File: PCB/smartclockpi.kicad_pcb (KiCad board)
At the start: 2 copper layers, 94.5 x 67.1 mm, 29 parts, among them J1 Raspberry_Pi, J2 DS3231 RTC module, J3 ILI9488 SPI TFT touchscreen, J5 USB_B_Micro, J6 USB_A, J7 microUSB IN, J8 USB-A OUT, J9 PWR IN, U2 MCP3008, U3 DHT22

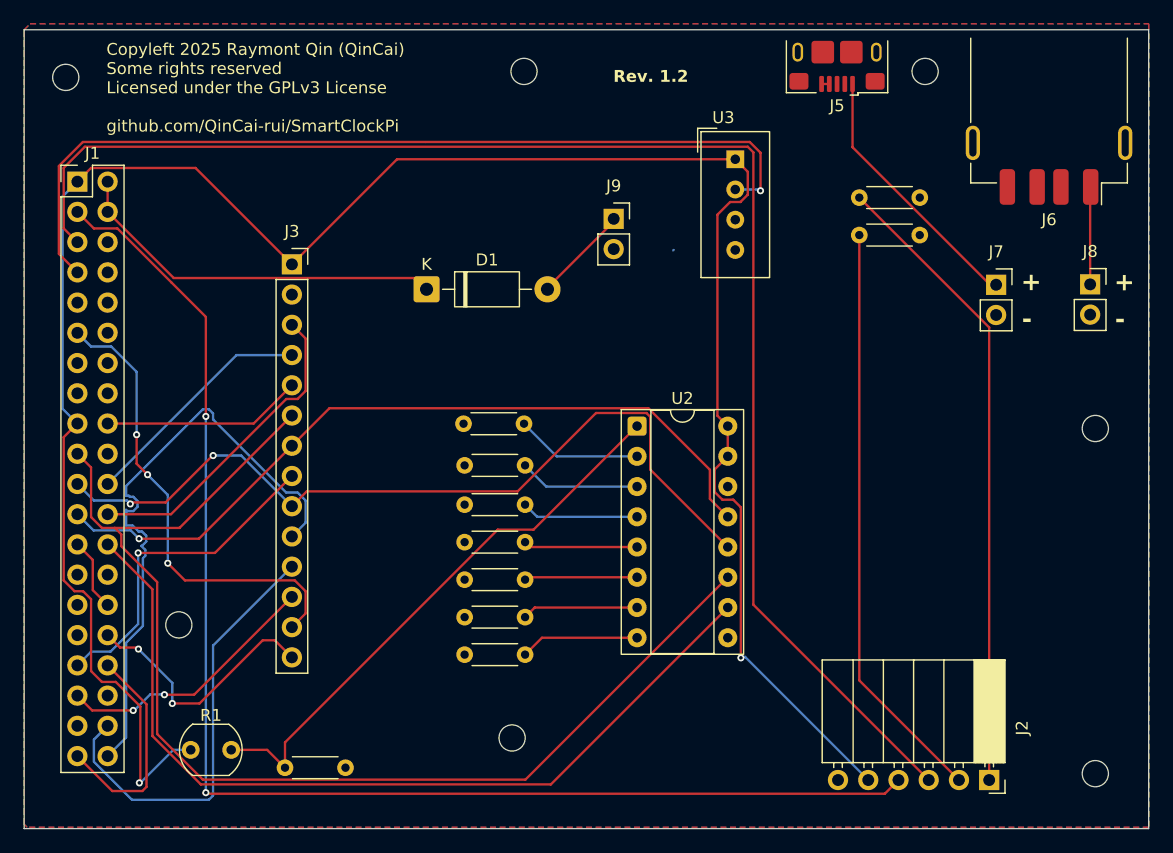
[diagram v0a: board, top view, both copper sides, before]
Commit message: fix PCB issues and re-gen everything needed
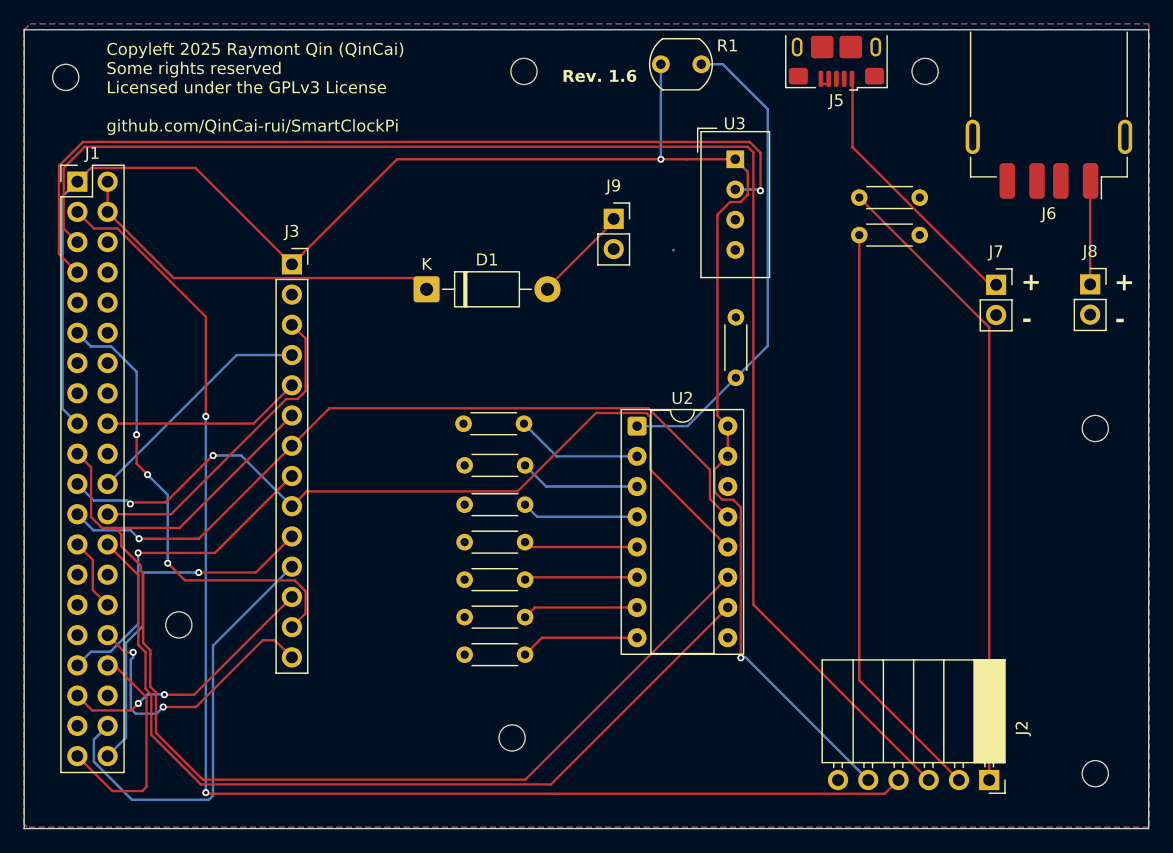
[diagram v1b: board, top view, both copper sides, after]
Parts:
- moved R1 69.8 mm to (93.5, 71.9)
- moved R2 50.1 mm to (99.8, 98.2), turned to 90 degrees
- moved J6 0.51 mm to (126.1, 74.5)
- moved J5 0.43 mm to (108.2, 70.5)
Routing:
- net +3.3V: track 185.3 -> 153.4 mm
- net Net-(J1-GPIO21/SCLK1): track 51.9 -> 30.4 mm, vias 0 -> 1
- net Net-(U2-CH0): track 47.9 -> 40.8 mm
- net Net-(J1-PWM0/GPIO12): track 21.7 -> 24.4 mm
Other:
- board text added: "Rev. 1.6"
- board text removed: "Rev. 1.2"

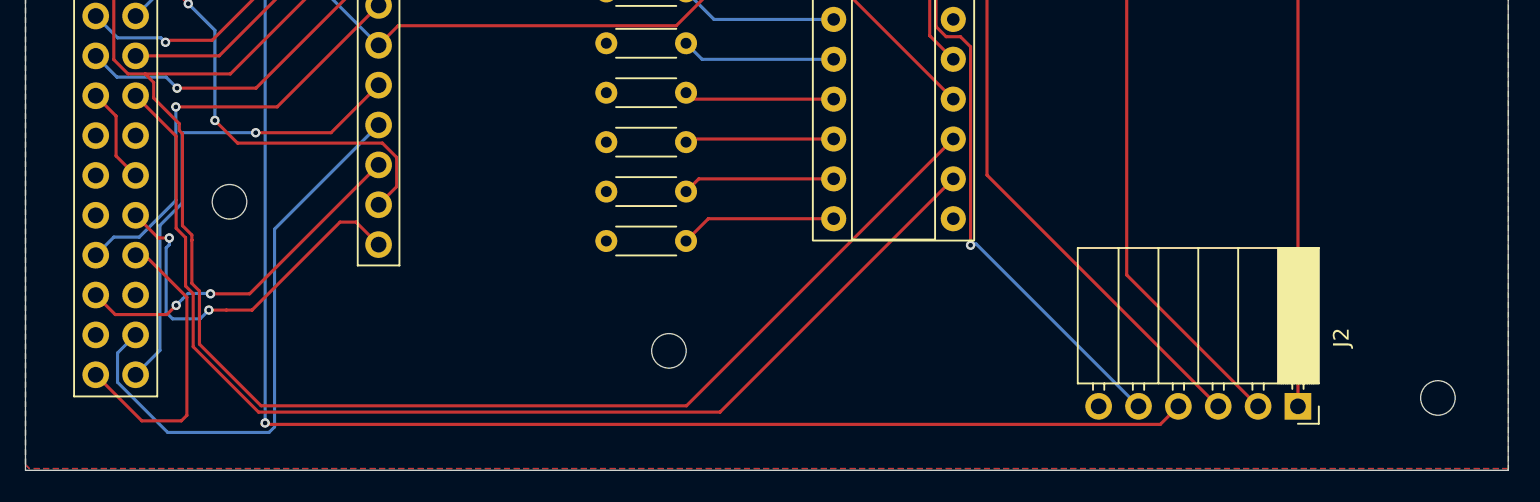
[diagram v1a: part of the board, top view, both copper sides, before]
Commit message: fix some DRC errors. regen models
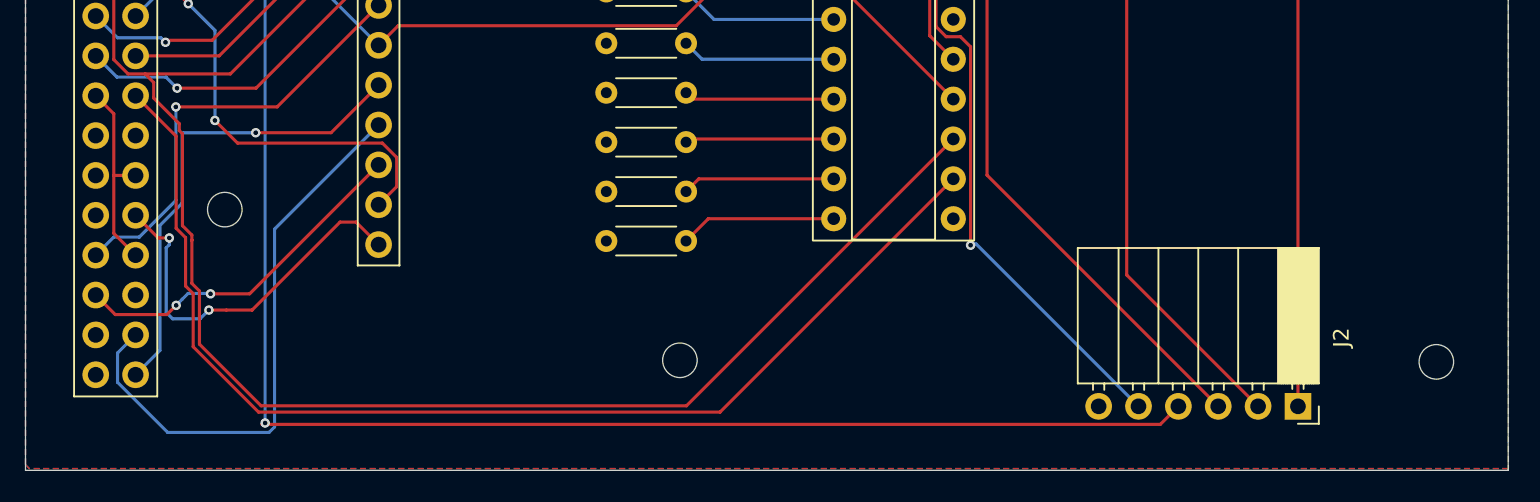
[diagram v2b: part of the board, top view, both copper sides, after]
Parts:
- moved REF** 2.30 mm to (129.9, 129.2)
- moved REF** 0.92 mm to (81.7, 129.1)
- moved REF** 0.58 mm to (52.7, 119.5)
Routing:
- net GND: track 26.4 -> 14.4 mm
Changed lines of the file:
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@@
 	(footprint "MountingHole:MountingHole_2.2mm_M2"
 		(layer "F.Cu")
-		(at 53 119)
+		(at 52.7 119.5)
 		(descr "Mounting Hole 2.2mm, M2, no annular, generated by kicad-footprint-generator mountinghole.py")
 		(tags "mountinghole M2")
@@
 	(footprint "MountingHole:MountingHole_2.2mm_M2"
 		(layer "F.Cu")
-		(at 81 128.5)
+		(at 81.7 129.1)
 		(descr "Mounting Hole 2.2mm, M2, no annular, generated by kicad-footprint-generator mountinghole.py")
 		(tags "mountinghole M2")
@@
 	(footprint "MountingHole:MountingHole_2.2mm_M2"
 		(layer "F.Cu")
+		(at 129.9 129.2)
+		(descr "Mounting Hole 2.2mm, M2, no annular, generated by kicad-footprint-generator mountinghole.py")
+		(tags "mountinghole M2")
+		(property "Reference" "REF**"
+			(at 0 -3.15 0)
+			(layer "F.SilkS")
+			(hide yes)
+			(effects
+				(font
+					(size 1 1)
+					(thickness 0.15)
+				)
+			)
+		)
+		(property "Value" "MountingHole_2.2mm_M2"
+			(at 0 3.15 0)
+			(layer "F.Fab")
+			(hide yes)
+			(effects
+				(font
+					(size 1 1)
+					(thickness 0.15)
+				)
+			)
+		)
+		(property "Datasheet" ""
+			(at 0 0 0)
+			(layer "F.Fab")
+			(hide yes)
+			(effects
+				(font
+					(size 1.27 1.27)
+					(thickness 0.15)
+				)
+			)
+		)
+		(property "Description" ""
+			(at 0 0 0)
+			(layer "F.Fab")
+			(hide yes)
+			(effects
+				(font
+					(size 1.27 1.27)
+					(thickness 0.15)
+				)
+			)
+		)
+		(attr exclude_from_pos_files exclude_from_bom)
+		(fp_circle
+			(center 0 0)
+			(end 2.2 0)
+			(stroke
+				(width 0.15)
+				(type solid)
+			)
+			(fill no)
+			(layer "Cmts.User")
+		)
+		(fp_circle
+			(center 0 0)
+			(end 2.45 0)
+			(stroke
+				(width 0.05)
+				(type solid)
+			)
+			(fill no)
+			(layer "F.CrtYd")
+		)
+		(fp_text user "${REFERENCE}"
+			(at 0 0 0)
+			(layer "F.Fab")
+			(effects
+				(font
+					(size 1 1)
+					(thickness 0.15)
+				)
+			)
+		)
+		(pad "" np_thru_hole circle
+			(at 0 0)
+			(size 2.2 2.2)
+			(drill 2.2)
+			(layers "*.Cu" "*.Mask")
+		)
+		(embedded_fonts no)
+	)
+	(footprint "MountingHole:MountingHole_2.2mm_M2"
+		(layer "F.Cu")
 		(at 43.5 73)
 		(descr "Mounting Hole 2.2mm, M2, no annular, generated by kicad-footprint-generator mountinghole.py")
@@
 		(embedded_fonts no)
 	)
-	(footprint "MountingHole:MountingHole_2.2mm_M2"
-		(layer "F.Cu")
-		(at 130 131.5)
-		(descr "Mounting Hole 2.2mm, M2, no annular, generated by kicad-footprint-generator mountinghole.py")
-		(tags "mountinghole M2")
-		(property "Reference" "REF**"
-			(at 0 -3.15 0)
-			(layer "F.SilkS")
-			(hide yes)
-			(effects
-				(font
-					(size 1 1)
-					(thickness 0.15)
-				)
-			)
-		)
-		(property "Value" "MountingHole_2.2mm_M2"
-			(at 0 3.15 0)
-			(layer "F.Fab")
-			(hide yes)
-			(effects
-				(font
-					(size 1 1)
-					(thickness 0.15)
-				)
-			)
-		)
-		(property "Datasheet" ""
-			(at 0 0 0)
-			(layer "F.Fab")
-			(hide yes)
-			(effects
-				(font
-					(size 1.27 1.27)
-					(thickness 0.15)
-				)
-			)
-		)
-		(property "Description" ""
-			(at 0 0 0)
-			(layer "F.Fab")
-			(hide yes)
-			(effects
-				(font
-					(size 1.27 1.27)
-					(thickness 0.15)
-				)
-			)
-		)
-		(attr exclude_from_pos_files exclude_from_bom)
-		(fp_circle
-			(center 0 0)
-			(end 2.2 0)
-			(stroke
-				(width 0.15)
-				(type solid)
-			)
-			(fill no)
-			(layer "Cmts.User")
-		)
-		(fp_circle
-			(center 0 0)
-			(end 2.45 0)
-			(stroke
-				(width 0.05)
-				(type solid)
-			)
-			(fill no)
-			(layer "F.CrtYd")
-		)
-		(fp_text user "${REFERENCE}"
-			(at 0 0 0)
-			(layer "F.Fab")
-			(effects
-				(font
-					(size 1 1)
-					(thickness 0.15)
-				)
-			)
-		)
-		(pad "" np_thru_hole circle
-			(at 0 0)
-			(size 2.2 2.2)
-			(drill 2.2)
-			(layers "*.Cu" "*.Mask")
-		)
-		(embedded_fonts no)
-	)
 	(gr_rect
 		(start 40 69)
@@
 	)
 	(segment
-		(start 45.7708 116.078)
-		(end 45.7708 113.538)
+		(start 47.0154 122.4026)
+		(end 47.6026 122.4026)
 		(width 0.2)
 		(layer "F.Cu")
@@
 	)
 	(segment
-		(start 47.0154 122.4026)
-		(end 47.6026 122.4026)
+		(start 45.6264 117.35)
+		(end 45.6264 113.3936)
 		(width 0.2)
 		(layer "F.Cu")
@@
 	)
 	(segment
-		(start 47.0154 117.3226)
-		(end 45.7708 116.078)
+		(start 45.6264 113.3936)
+		(end 44.4754 112.2426)
 		(width 0.2)
 		(layer "F.Cu")
@@
 	)
 	(segment
-		(start 45.7708 113.538)
-		(end 44.4754 112.2426)
+		(start 45.6264 121.0136)
+		(end 45.6264 117.35)
 		(width 0.2)
 		(layer "F.Cu")
@@
 	)
 	(segment
-		(start 49.931343 132.9604)
-		(end 47.4132 132.9604)
+		(start 45.6538 117.3226)
+		(end 45.6264 117.35)
 		(width 0.2)
 		(layer "F.Cu")
@@
 	)
 	(segment
-		(start 47.4132 132.9604)
-		(end 44.4754 130.0226)
-		(width 0.2)
-		(layer "F.Cu")
-		(net 1)
-	)
-	(segment
-		(start 47.6026 122.4026)
-		(end 50.2834 125.0834)
-		(width 0.2)
-		(layer "F.Cu")
-		(net 1)
-	)
-	(segment
-		(start 50.2834 125.0834)
-		(end 50.2834 132.608343)
+		(start 47.0154 122.4026)
+		(end 45.6264 121.0136)
 		(width 0.2)
 		(layer "F.Cu")
@@
 	)
 	(segment
-		(start 50.2834 132.608343)
-		(end 49.931343 132.9604)
+		(start 47.0154 117.3226)
+		(end 45.6538 117.3226)
 		(width 0.2)
 		(layer "F.Cu")

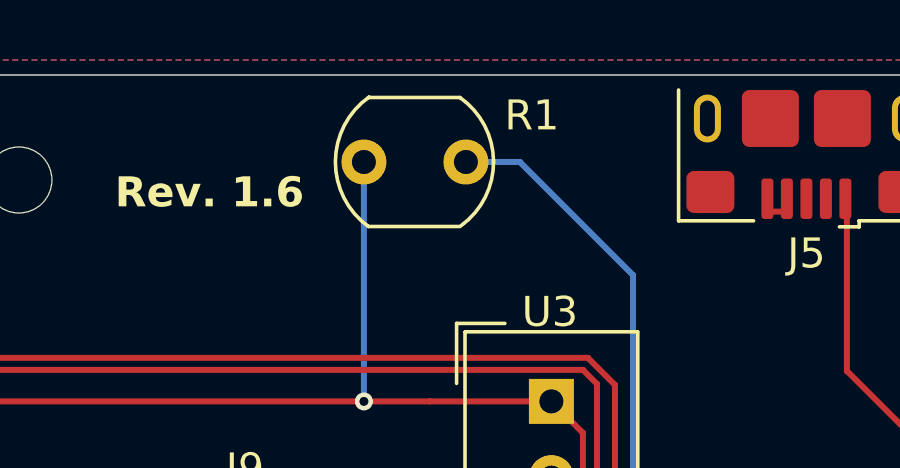
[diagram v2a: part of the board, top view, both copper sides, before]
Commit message: update footprint for LDR. re-gen models
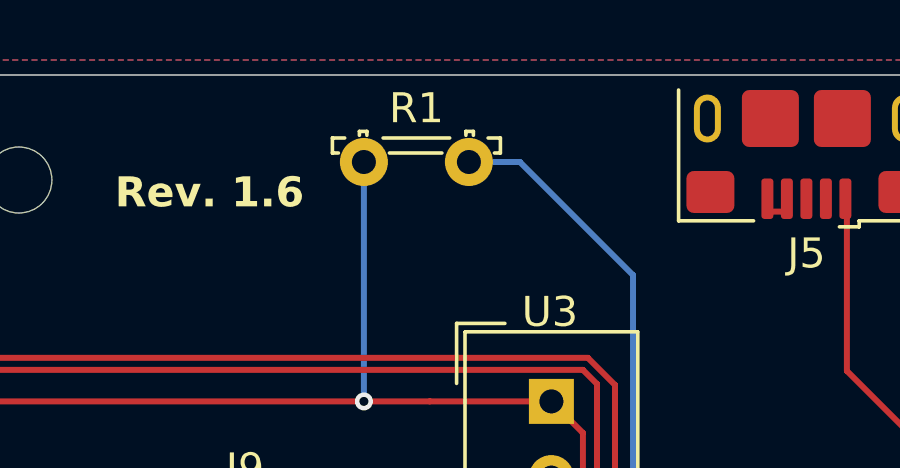
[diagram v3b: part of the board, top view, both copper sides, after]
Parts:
- R1: footprint OptoDevice:R_LDR_5.1x4.3mm_P3.4mm_Vertical -> OptoDevice:R_LDR_5.2x5.2mm_P3.5mm_Horizontal
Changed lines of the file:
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@@
 		)
 	)
-	(footprint "OptoDevice:R_LDR_5.1x4.3mm_P3.4mm_Vertical"
+	(footprint "OptoDevice:R_LDR_5.2x5.2mm_P3.5mm_Horizontal"
 		(layer "F.Cu")
 		(at 93.5 71.9)
-		(descr "Resistor, LDR 5.1x3.4mm, see http://yourduino.com/docs/Photoresistor-5516-datasheet.pdf")
-		(tags "Resistor LDR5.1x3.4mm")
+		(descr "Resistor, LDR 5.2x5.2, upright, see http://cdn-reichelt.de/documents/datenblatt/A500/M996011A.pdf")
+		(tags "Resistor LDR5.2x5.2 ")
 		(property "Reference" "R1"
-			(at 5.6 -1.55 0)
+			(at 1.75 -1.79 0)
 			(layer "F.SilkS")
 			(effects
@@
 		)
 		(property "Value" "LDR07"
-			(at 1.5 3 0)
+			(at 1.62 1.4 0)
 			(layer "F.Fab")
 			(effects
@@
 		(attr through_hole)
 		(fp_line
-			(start 0.15 -2.15)
-			(end 3.2 -2.15)
-			(stroke
-				(width 0.12)
-				(type solid)
-			)
-			(layer "F.SilkS")
-		)
-		(fp_line
-			(start 0.15 2.15)
-			(end 3.2 2.15)
-			(stroke
-				(width 0.12)
-				(type solid)
-			)
-			(layer "F.SilkS")
-		)
-		(fp_arc
-			(start 0.15 2.15)
-			(mid -0.950438 -0.013368)
-			(end 0.171766 -2.165525)
-			(stroke
-				(width 0.12)
-				(type solid)
-			)
-			(layer "F.SilkS")
-		)
-		(fp_arc
-			(start 3.2 -2.15)
-			(mid 4.321403 -0.027338)
-			(end 3.244513 2.118249)
-			(stroke
-				(width 0.12)
-				(type solid)
-			)
-			(layer "F.SilkS")
-		)
-		(fp_line
-			(start -1.13 -2.35)
-			(end -1.13 2.35)
+			(start -1.05 -0.8)
+			(end -1.05 -0.3)
+			(stroke
+				(width 0.12)
+				(type solid)
+			)
+			(layer "F.SilkS")
+		)
+		(fp_line
+			(start -1.05 -0.3)
+			(end -0.85 -0.3)
+			(stroke
+				(width 0.12)
+				(type solid)
+			)
+			(layer "F.SilkS")
+		)
+		(fp_line
+			(start -0.64 -0.8)
+			(end -1.05 -0.8)
+			(stroke
+				(width 0.12)
+				(type solid)
+			)
+			(layer "F.SilkS")
+		)
+		(fp_line
+			(start -0.15 -1.02)
+			(end -0.15 -0.89)
+			(stroke
+				(width 0.12)
+				(type solid)
+			)
+			(layer "F.SilkS")
+		)
+		(fp_line
+			(start -0.15 -1.02)
+			(end 0.1 -1.02)
+			(stroke
+				(width 0.12)
+				(type solid)
+			)
+			(layer "F.SilkS")
+		)
+		(fp_line
+			(start 0.1 -1.02)
+			(end 0.1 -0.89)
+			(stroke
+				(width 0.12)
+				(type solid)
+			)
+			(layer "F.SilkS")
+		)
+		(fp_line
+			(start 0.85 -0.3)
+			(end 2.6 -0.3)
+			(stroke
+				(width 0.12)
+				(type solid)
+			)
+			(layer "F.SilkS")
+		)
+		(fp_line
+			(start 2.86 -0.8)
+			(end 0.64 -0.8)
+			(stroke
+				(width 0.12)
+				(type solid)
+			)
+			(layer "F.SilkS")
+		)
+		(fp_line
+			(start 3.4 -1.02)
+			(end 3.4 -0.89)
+			(stroke
+				(width 0.12)
+				(type solid)
+			)
+			(layer "F.SilkS")
+		)
+		(fp_line
+			(start 3.4 -1.02)
+			(end 3.65 -1.02)
+			(stroke
+				(width 0.12)
+				(type solid)
+			)
+			(layer "F.SilkS")
+		)
+		(fp_line
+			(start 3.65 -1.02)
+			(end 3.65 -0.89)
+			(stroke
+				(width 0.12)
+				(type solid)
+			)
+			(layer "F.SilkS")
+		)
+		(fp_line
+			(start 4.35 -0.3)
+			(end 4.55 -0.3)
+			(stroke
+				(width 0.12)
+				(type solid)
+			)
+			(layer "F.SilkS")
+		)
+		(fp_line
+			(start 4.55 -0.8)
+			(end 4.14 -0.8)
+			(stroke
+				(width 0.12)
+				(type solid)
+			)
+			(layer "F.SilkS")
+		)
+		(fp_line
+			(start 4.55 -0.3)
+			(end 4.55 -0.8)
+			(stroke
+				(width 0.12)
+				(type solid)
+			)
+			(layer "F.SilkS")
+		)
+		(fp_line
+			(start -1.25 -1.15)
+			(end -1.25 1.05)
 			(stroke
 				(width 0.05)
@@
 		)
 		(fp_line
-			(start -1.13 -2.35)
-			(end 4.53 -2.35)
+			(start -1.25 -1.15)
+			(end 4.75 -1.15)
 			(stroke
 				(width 0.05)
@@
 		)
 		(fp_line
-			(start 4.53 2.35)
-			(end -1.13 2.35)
+			(start 4.75 1.05)
+			(end -1.25 1.05)
 			(stroke
 				(width 0.05)
@@
 		)
 		(fp_line
-			(start 4.53 2.35)
-			(end 4.53 -2.35)
+			(start 4.75 1.05)
+			(end 4.75 -1.15)
 			(stroke
 				(width 0.05)
@@
 		)
 		(fp_line
-			(start 0.2 -2.1)
-			(end 3.2 -2.1)
-			(stroke
-				(width 0.1)
-				(type solid)
-			)
-			(layer "F.Fab")
-		)
-		(fp_line
-			(start 0.8 -1.8)
-			(end 2.6 -1.8)
-			(stroke
-				(width 0.1)
-				(type solid)
-			)
-			(layer "F.Fab")
-		)
-		(fp_line
-			(start 0.8 -1.2)
-			(end 0.8 -0.6)
-			(stroke
-				(width 0.1)
-				(type solid)
-			)
-			(layer "F.Fab")
-		)
-		(fp_line
-			(start 0.8 1.2)
-			(end 0.8 1.8)
-			(stroke
-				(width 0.1)
-				(type solid)
-			)
-			(layer "F.Fab")
-		)
-		(fp_line
-			(start 0.8 1.8)
-			(end 2.6 1.8)
-			(stroke
-				(width 0.1)
-				(type solid)
-			)
-			(layer "F.Fab")
-		)
-		(fp_line
-			(start 1 0)
-			(end 1 0.6)
-			(stroke
-				(width 0.1)
-				(type solid)
-			)
-			(layer "F.Fab")
-		)
-		(fp_line
-			(start 1 0)
-			(end 2.3 0)
-			(stroke
-				(width 0.1)
-				(type solid)
-			)
-			(layer "F.Fab")
-		)
-		(fp_line
-			(start 2.3 -0.6)
-			(end 0.8 -0.6)
-			(stroke
-				(width 0.1)
-				(type solid)
-			)
-			(layer "F.Fab")
-		)
-		(fp_line
-			(start 2.3 0)
-			(end 2.3 -0.6)
-			(stroke
-				(width 0.1)
-				(type solid)
-			)
-			(layer "F.Fab")
-		)
-		(fp_line
-			(start 2.6 -1.8)
-			(end 2.6 -1.2)
-			(stroke
-				(width 0.1)
-				(type solid)
-			)
-			(layer "F.Fab")
-		)
-		(fp_line
-			(start 2.6 -1.2)
-			(end 0.8 -1.2)
-			(stroke
-				(width 0.1)
-				(type solid)
-			)
-			(layer "F.Fab")
-		)
-		(fp_line
-			(start 2.6 0.6)
-			(end 1 0.6)
-			(stroke
-				(width 0.1)
-				(type solid)
-			)
-			(layer "F.Fab")
-		)
-		(fp_line
-			(start 2.6 0.6)
-			(end 2.6 1.2)
-			(stroke
-				(width 0.1)
-				(type solid)
-			)
-			(layer "F.Fab")
-		)
-		(fp_line
-			(start 2.6 1.2)
-			(end 0.8 1.2)
-			(stroke
-				(width 0.1)
-				(type solid)
-			)
-			(layer "F.Fab")
-		)
-		(fp_line
-			(start 3.2 2.1)
-			(end 0.2 2.1)
-			(stroke
-				(width 0.1)
-				(type solid)
-			)
-			(layer "F.Fab")
-		)
-		(fp_arc
-			(start 0.2 2.1)
-			(mid -0.880697 -0.001697)
-			(end 0.202763 -2.101971)
-			(stroke
-				(width 0.1)
-				(type solid)
-			)
-			(layer "F.Fab")
-		)
-		(fp_arc
-			(start 3.2 -2.1)
-			(mid 4.280697 0.001697)
-			(end 3.197237 2.101971)
-			(stroke
-				(width 0.1)
-				(type solid)
-			)
-			(layer "F.Fab")
+			(start -1 -0.75)
+			(end 4.5 -0.75)
+			(stroke
+				(width 0.1)
+				(type solid)
+			)
+			(layer "F.Fab")
+		)
+		(fp_line
+			(start -1 -0.35)
+			(end -1 -0.75)
+			(stroke
+				(width 0.1)
+				(type solid)
+			)
+			(layer "F.Fab")
+		)
+		(fp_line
+			(start 0 0)
+			(end 0 -0.9)
+			(stroke
+				(width 0.1)
+				(type solid)
+			)
+			(layer "F.Fab")
+		)
+		(fp_line
+			(start 3.5 0)
+			(end 3.5 -0.9)
+			(stroke
+				(width 0.1)
+				(type solid)
+			)
+			(layer "F.Fab")
+		)
+		(fp_line
+			(start 4.5 -0.75)
+			(end 4.5 -0.35)
+			(stroke
+				(width 0.1)
+				(type solid)
+			)
+			(layer "F.Fab")
+		)
+		(fp_line
+			(start 4.5 -0.35)
+			(end -1 -0.35)
+			(stroke
+				(width 0.1)
+				(type solid)
+			)
+			(layer "F.Fab")
+		)
+		(fp_text user "${REFERENCE}"
+			(at 1.75 -1.79 0)
+			(layer "F.Fab")
+			(effects
+				(font
+					(size 1 1)
+					(thickness 0.15)
+				)
+			)
 		)
 		(pad "1" thru_hole circle
 			(at 0 0)
-			(size 1.5 1.5)
+			(size 1.6 1.6)
 			(drill 0.8)
 			(layers "*.Cu" "*.Mask")
@@
 		)
 		(pad "2" thru_hole circle
-			(at 3.4 0)
-			(size 1.5 1.5)
+			(at 3.5 0)
+			(size 1.6 1.6)
 			(drill 0.8)
 			(layers "*.Cu" "*.Mask")
@@
 		)
 		(embedded_fonts no)
-		(model "${KICAD9_3DMODEL_DIR}/OptoDevice.3dshapes/R_LDR_5.1x4.3mm_P3.4mm_Vertical.step"
+		(model "${KICAD9_3DMODEL_DIR}/OptoDevice.3dshapes/R_LDR_5.2x5.2mm_P3.5mm_Horizontal.step"
 			(offset
 				(xyz 0 0 0)
